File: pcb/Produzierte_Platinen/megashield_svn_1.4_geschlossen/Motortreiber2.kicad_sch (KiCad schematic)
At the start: 4 parts

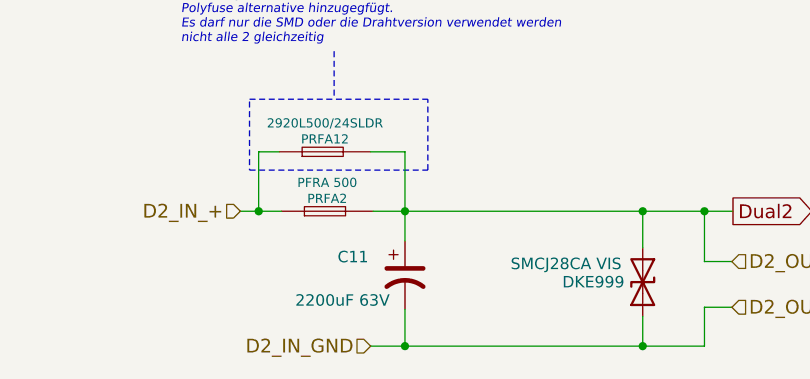
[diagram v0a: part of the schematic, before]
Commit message: megashield_svn_1.4_geschlossen - für Kicad 6.99 angepasst
megashield_svn_1.4_geschlossen für Kicad 6.99 angepasst
Es wurden keine anderen Änderungen am Schaltplan, Platinen Layout oder sonstiges vorgenommen.
Die  vorgenommen Änderungen betreffen nur das Dateiformat von Kicad V6.99 und das ändern der Ordnerpfade zu den Footprints, LIberty und den 3D Modellen
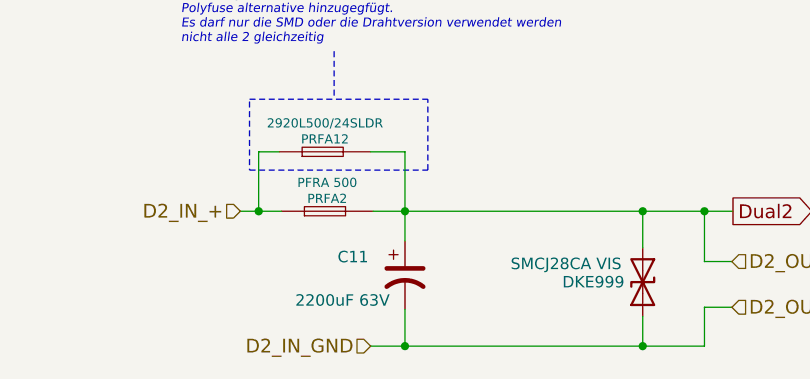
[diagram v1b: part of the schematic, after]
